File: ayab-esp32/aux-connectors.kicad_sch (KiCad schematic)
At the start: 22 parts, among them J403 AYAB_I2C, J403 AYAB_UART, J403 USER_I2C, J404 AYAB_SPI, J802 I2C_VBUS, Q801 AO3400A, Q802 AO3400A

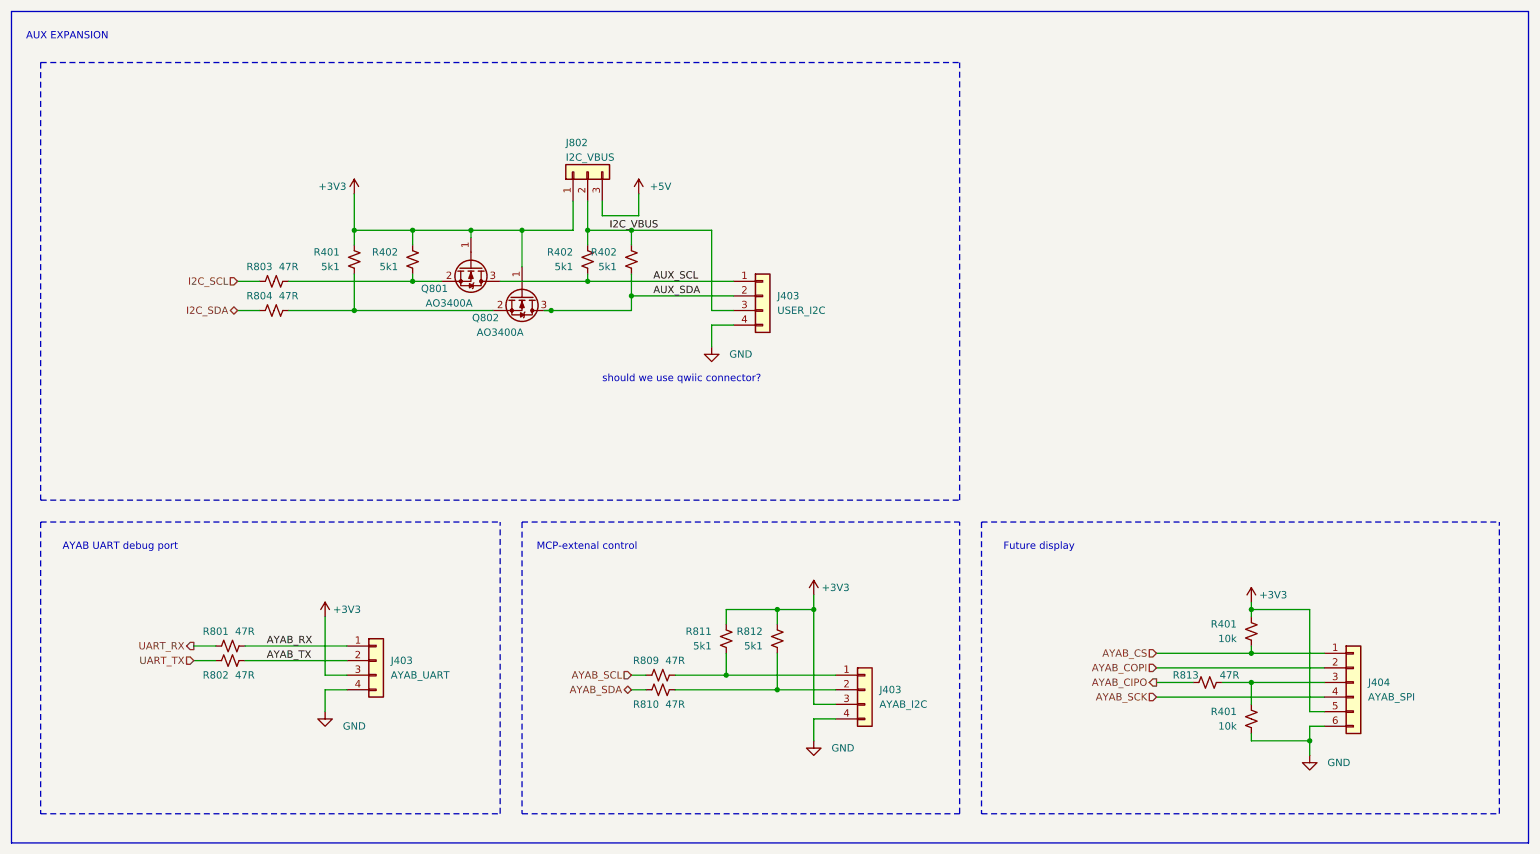
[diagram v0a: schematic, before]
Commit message: i2c0 level-shifter
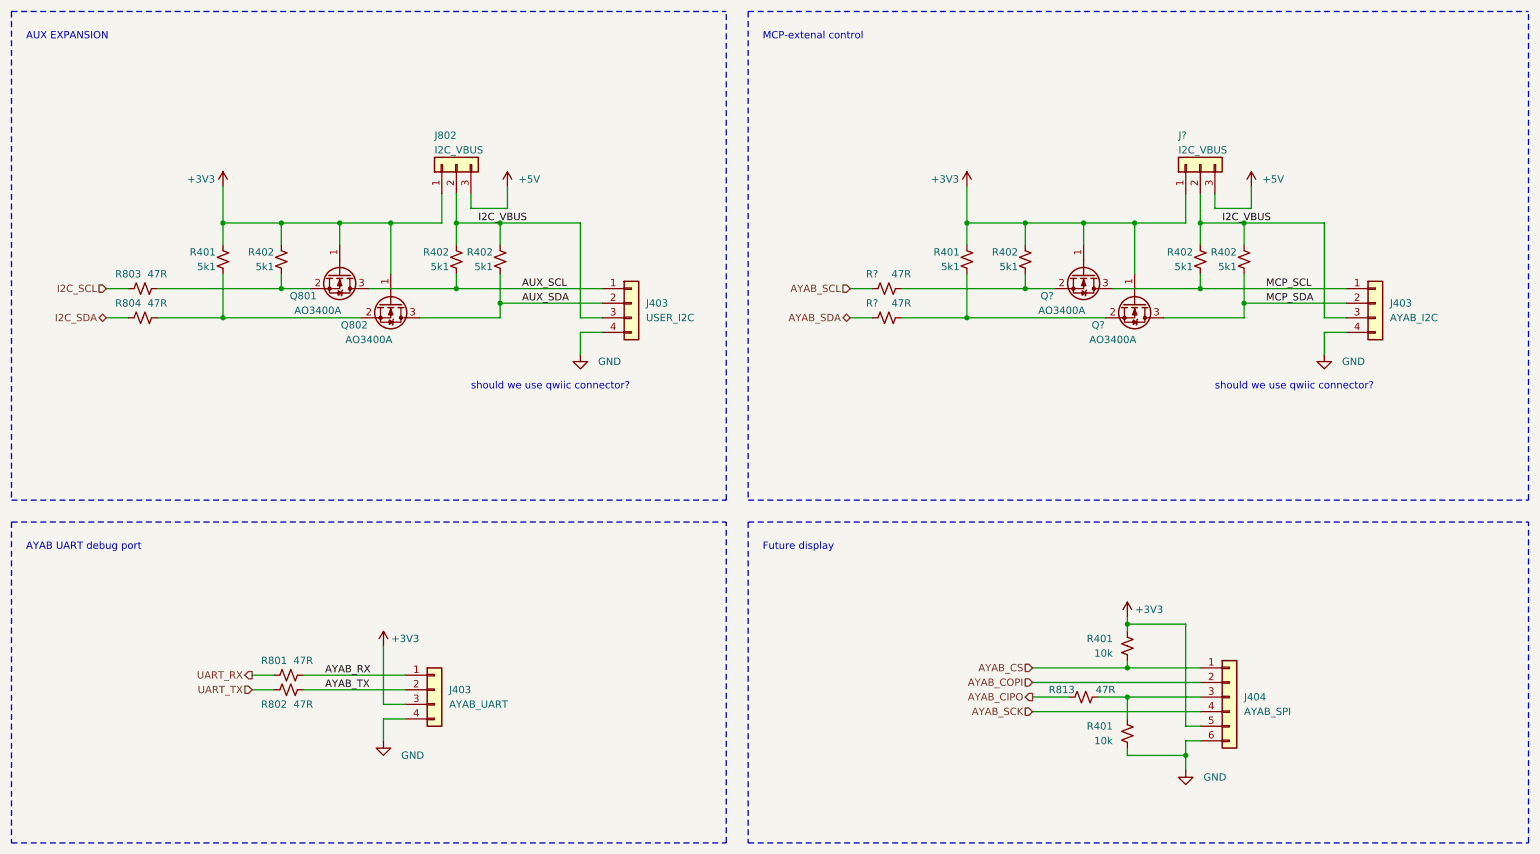
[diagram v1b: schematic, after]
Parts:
- removed R809, R810: 47R, symbol ayab-esp32:R_Small_US
- removed R811, R812: 5k1, symbol ayab-esp32:R_Small_US
- added J?: I2C_VBUS, symbol ayab-esp32:Conn_01x03
- added Q? (x2): AO3400A, Package_TO_SOT_SMD:SOT-23, symbol ayab-esp32:AO3400A
- added R401, R402 (x3): 5k1, symbol ayab-esp32:R_Small_US
- added R? (x2): 47R, symbol ayab-esp32:R_Small_US
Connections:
- net +3V3: now also J?.1 (Pin_1), Q?.1 (G), Q?.1 (G), R401.1, R402.1; no longer J403.3 (Pin_3)
- net +5V: now also J?.3 (Pin_3)
- net AYAB_SCL: now also R?.1
- net AYAB_SDA: now also R?.1
- net I2C_VBUS: now also J403.3 (Pin_3), J?.2 (Pin_2), R402.1, R402.1
- net MCP_SDA: now reaches J403.2 (Pin_2)
- net MCP_SDA: now also Q?.3 (D), R402.2
- net MCP_SCL: now reaches J403.1 (Pin_1)
- net MCP_SCL: now also Q?.3 (D), R402.2
- new net: Q?.2 (S), R401.2, R?.2
- new net: Q?.2 (S), R402.2, R?.2
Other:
- moved on the sheet: J403, J404, J802, Q801, Q802, R401, R402, R801, R802, R803, R804, R813

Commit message: work on BOM and parts selection
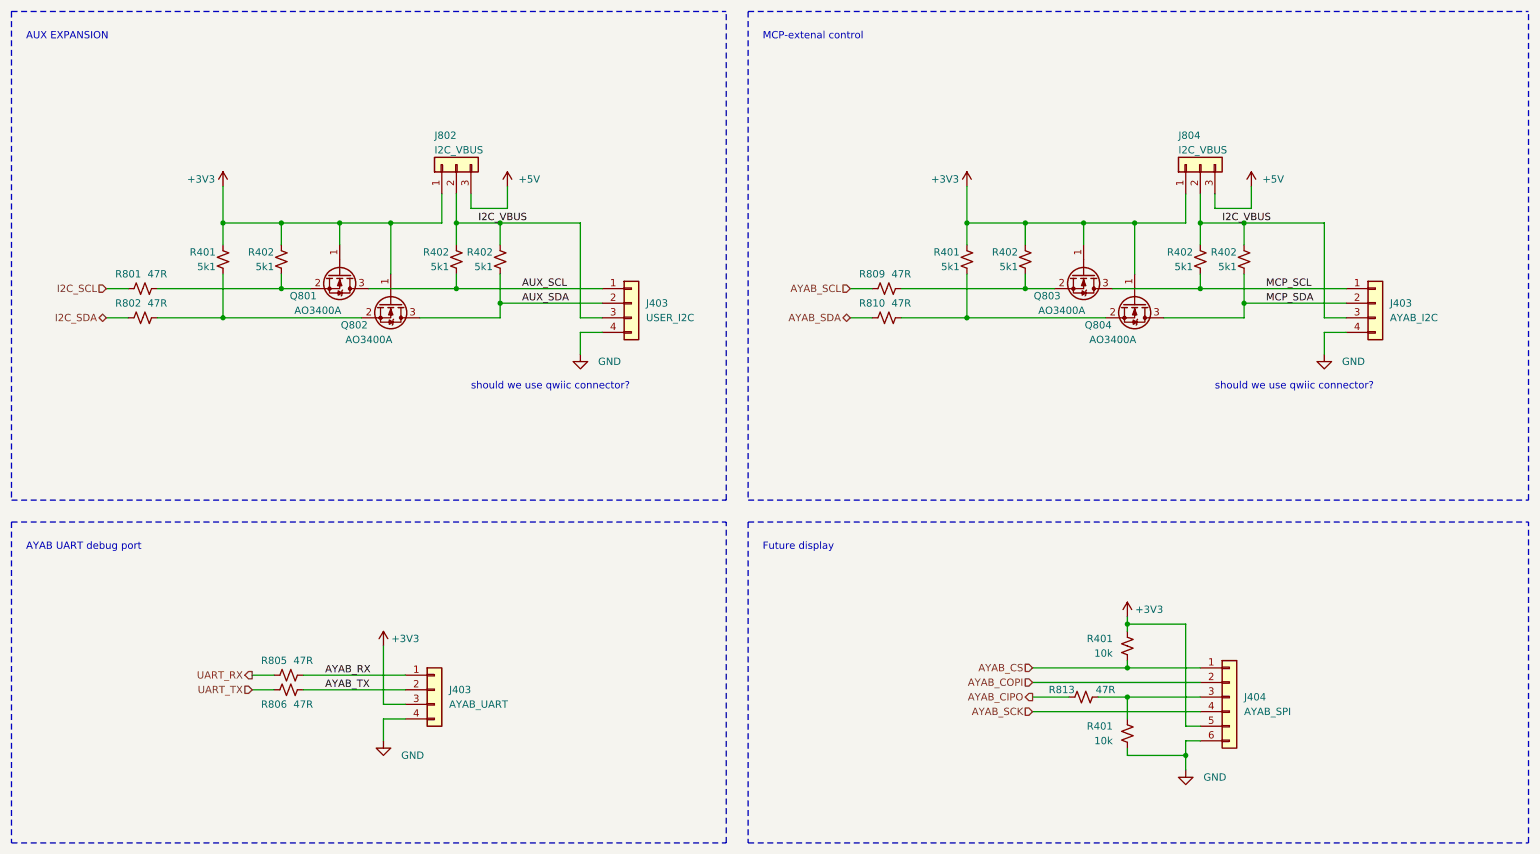
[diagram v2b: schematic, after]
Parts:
- J403: footprint (none) -> Connector_PinHeader_2.54mm:PinHeader_1x04_P2.54mm_Vertical; symbol ayab-esp32:Conn_01x04 -> Library:Conn_01x04; LCSC ID (none) -> C3029334; OEM (none) -> XUNPU; OEM PN (none) -> WAFER-SH1.0-4PLB
- J403: footprint (none) -> Connector_JST:JST_SH_SM04B-SRSS-TB_1x04-1MP_P1.00mm_Horizontal; symbol ayab-esp32:Conn_01x04 -> Library:Conn_01x04; LCSC ID (none) -> C3029334; OEM (none) -> XUNPU; OEM PN (none) -> WAFER-SH1.0-4PLB
- J403: footprint (none) -> Connector_PinSocket_2.54mm:PinSocket_1x04_P2.54mm_Vertical; symbol ayab-esp32:Conn_01x04 -> Library:Conn_01x04; LCSC ID (none) -> C3029334; OEM (none) -> XUNPU; OEM PN (none) -> WAFER-SH1.0-4PLB
- J404: footprint (none) -> Connector_JST:JST_SH_SM06B-SRSS-TB_1x06-1MP_P1.00mm_Horizontal; symbol ayab-esp32:Conn_01x06 -> Library:Conn_01x06; LCSC ID (none) -> C3029345; OEM (none) -> XUNPU; OEM PN (none) -> WAFER-SH1.0-6PWB
- J802: footprint (none) -> Jumper:SolderJumper-3_P1.3mm_Bridged12_RoundedPad1.0x1.5mm; symbol ayab-esp32:Conn_01x03 -> Library:Conn_01x03
- J804: renamed from J?; footprint (none) -> Jumper:SolderJumper-3_P1.3mm_Bridged12_RoundedPad1.0x1.5mm; symbol ayab-esp32:Conn_01x03 -> Library:Conn_01x03
- Q801, Q802: symbol ayab-esp32:AO3400A -> Library:AO3400A; LCSC ID (none) -> C20917; OEM (none) -> Alpha & Omega Semicon; OEM PN (none) -> AO3400A; Package (none) -> SOT-23
- Q803, Q804: renamed from Q?; symbol ayab-esp32:AO3400A -> Library:AO3400A; LCSC ID (none) -> C20917; OEM (none) -> Alpha & Omega Semicon; OEM PN (none) -> AO3400A; Package (none) -> SOT-23
- R401, R402: footprint (none) -> Resistor_SMD:R_0603_1608Metric; symbol ayab-esp32:R_Small_US -> Library:R_Small_US; LCSC ID (none) -> C23186; OEM (none) -> UNI-ROYAL(Uniroyal Elec); OEM PN (none) -> 0603WAF5101T5E; Package (none) -> 0603
- R401: footprint (none) -> Resistor_SMD:R_0603_1608Metric; symbol ayab-esp32:R_Small_US -> Library:R_Small_US; LCSC ID (none) -> C25804; OEM (none) -> UNI-ROYAL(Uniroyal Elec); OEM PN (none) -> 0603WAF1002T5E; Package (none) -> 0603
- R801: renamed from R803; footprint (none) -> Resistor_SMD:R_0603_1608Metric; symbol ayab-esp32:R_Small_US -> Library:R_Small_US; LCSC ID (none) -> C23182; OEM (none) -> UNI-ROYAL(Uniroyal Elec); OEM PN (none) -> 0603WAF470JT5E; Package (none) -> 0603
- R802: renamed from R804; footprint (none) -> Resistor_SMD:R_0603_1608Metric; symbol ayab-esp32:R_Small_US -> Library:R_Small_US; LCSC ID (none) -> C23182; OEM (none) -> UNI-ROYAL(Uniroyal Elec); OEM PN (none) -> 0603WAF470JT5E; Package (none) -> 0603
- R805: renamed from R801; footprint (none) -> Resistor_SMD:R_0603_1608Metric; symbol ayab-esp32:R_Small_US -> Library:R_Small_US; LCSC ID (none) -> C23182; OEM (none) -> UNI-ROYAL(Uniroyal Elec); OEM PN (none) -> 0603WAF470JT5E; Package (none) -> 0603
- R806: renamed from R802; footprint (none) -> Resistor_SMD:R_0603_1608Metric; symbol ayab-esp32:R_Small_US -> Library:R_Small_US; LCSC ID (none) -> C23182; OEM (none) -> UNI-ROYAL(Uniroyal Elec); OEM PN (none) -> 0603WAF470JT5E; Package (none) -> 0603
- R809, R810: renamed from R?; footprint (none) -> Resistor_SMD:R_0603_1608Metric; symbol ayab-esp32:R_Small_US -> Library:R_Small_US; LCSC ID (none) -> C23182; OEM (none) -> UNI-ROYAL(Uniroyal Elec); OEM PN (none) -> 0603WAF470JT5E; Package (none) -> 0603
- R813: footprint (none) -> Resistor_SMD:R_0603_1608Metric; symbol ayab-esp32:R_Small_US -> Library:R_Small_US; LCSC ID (none) -> C23182; OEM (none) -> UNI-ROYAL(Uniroyal Elec); OEM PN (none) -> 0603WAF470JT5E; Package (none) -> 0603
